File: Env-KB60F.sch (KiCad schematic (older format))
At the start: 125 parts, among them U1 Pico

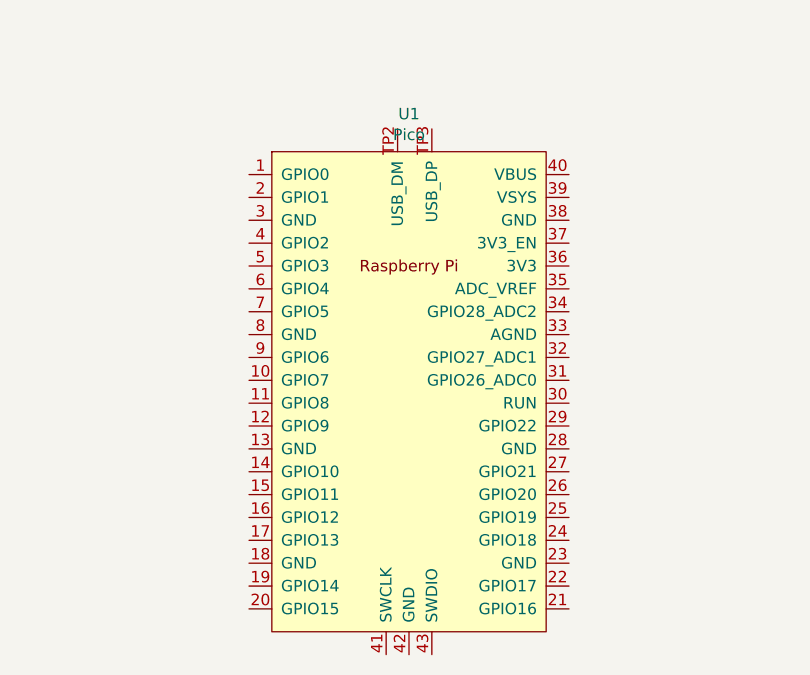
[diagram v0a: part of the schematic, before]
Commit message: Diodes were wrong direction
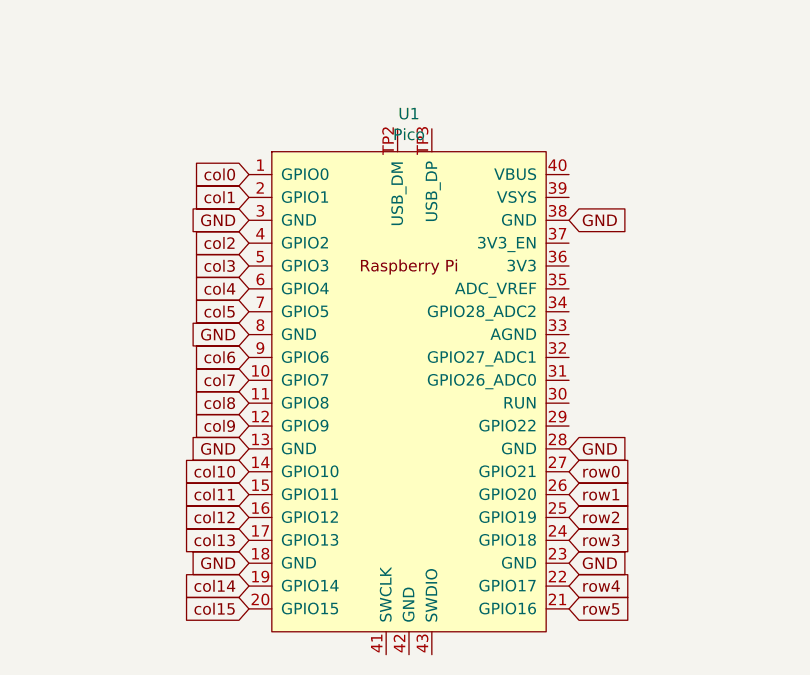
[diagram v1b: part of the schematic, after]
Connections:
- net col0: now also U1.1 (GPIO0)
- net col1: now also U1.2 (GPIO1)
- net col10: now also U1.14 (GPIO10)
- net col11: now also U1.15 (GPIO11)
- net col12: now also U1.16 (GPIO12)
- net col13: now also U1.17 (GPIO13)
- net col14: now also U1.19 (GPIO14)
- net col2: now also U1.4 (GPIO2)
- net col3: now also U1.5 (GPIO3)
- net col4: now also U1.6 (GPIO4)
- net col5: now also U1.7 (GPIO5)
- net col6: now also U1.9 (GPIO6)
- net col7: now also U1.10 (GPIO7)
- net col8: now also U1.11 (GPIO8)
- net col9: now also U1.12 (GPIO9)
- net row0: now also U1.27 (GPIO21)
- net row1: now also U1.26 (GPIO20)
- net row2: now also U1.25 (GPIO19)
- net row3: now also U1.24 (GPIO18)
- net row4: now also U1.22 (GPIO17)
- net GND: now reaches U1.13 (GND)
- net GND: now also U1.18 (GND), U1.23 (GND), U1.28 (GND), U1.3 (GND), U1.38 (GND), U1.8 (GND)
- net col15: now reaches U1.20 (GPIO15)
- net row5: now reaches U1.21 (GPIO16)
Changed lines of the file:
@@
 	1    0    0    -1
 $EndComp
+Text GLabel 3100 6950 0    50   Input ~ 0
+GND
+Text GLabel 3100 7450 0    50   Input ~ 0
+GND
+Text GLabel 3100 7950 0    50   Input ~ 0
+GND
+Text GLabel 3100 6450 0    50   Input ~ 0
+GND
+Text GLabel 4500 6450 2    50   Input ~ 0
+GND
+Text GLabel 4500 7450 2    50   Input ~ 0
+GND
+Text GLabel 4500 7950 2    50   Input ~ 0
+GND
+Text GLabel 4500 7550 2    50   Input ~ 0
+row0
+Text GLabel 4500 7650 2    50   Input ~ 0
+row1
+Text GLabel 4500 7750 2    50   Input ~ 0
+row2
+Text GLabel 4500 7850 2    50   Input ~ 0
+row3
+Text GLabel 4500 8050 2    50   Input ~ 0
+row4
+Text GLabel 4500 8150 2    50   Input ~ 0
+row5
+Text GLabel 3100 6250 0    50   Input ~ 0
+col0
+Text GLabel 3100 6350 0    50   Input ~ 0
+col1
+Text GLabel 3100 6550 0    50   Input ~ 0
+col2
+Text GLabel 3100 6650 0    50   Input ~ 0
+col3
+Text GLabel 3100 6750 0    50   Input ~ 0
+col4
+Text GLabel 3100 6850 0    50   Input ~ 0
+col5
+Text GLabel 3100 7050 0    50   Input ~ 0
+col6
+Text GLabel 3100 7150 0    50   Input ~ 0
+col7
+Text GLabel 3100 7250 0    50   Input ~ 0
+col8
+Text GLabel 3100 7350 0    50   Input ~ 0
+col9
+Text GLabel 3100 7550 0    50   Input ~ 0
+col10
+Text GLabel 3100 7650 0    50   Input ~ 0
+col11
+Text GLabel 3100 7750 0    50   Input ~ 0
+col12
+Text GLabel 3100 7850 0    50   Input ~ 0
+col13
+Text GLabel 3100 8050 0    50   Input ~ 0
+col14
+Text GLabel 3100 8150 0    50   Input ~ 0
+col15
 $EndSCHEMATC

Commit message: General Re-doing of stuff
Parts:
- added H? (x6): MountingHole, symbol Mechanical:MountingHole
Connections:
- net col15 is gone; now on net row4: U1.20 (GPIO15)
- net row5 is gone; now on net col6: U1.21 (GPIO16)
- net col0: now also U1.14 (GPIO10); no longer U1.1 (GPIO0)
- net col1: now also U1.12 (GPIO9); no longer U1.2 (GPIO1)
- net col10: now also U1.26 (GPIO20); no longer U1.14 (GPIO10)
- net col11: now also U1.27 (GPIO21); no longer U1.15 (GPIO11)
- net col12: now also U1.29 (GPIO22); no longer U1.16 (GPIO12)
- net col13: now also U1.31 (GPIO26_ADC0); no longer U1.17 (GPIO13)
- net col14: now also U1.32 (GPIO27_ADC1); no longer U1.19 (GPIO14)
- net col2: now also U1.11 (GPIO8); no longer U1.4 (GPIO2)
- net col3: now also U1.10 (GPIO7); no longer U1.5 (GPIO3)
- net col4: now also U1.9 (GPIO6); no longer U1.6 (GPIO4)
- net col6: no longer U1.9 (GPIO6)
- net col7: now also U1.22 (GPIO17); no longer U1.10 (GPIO7)
- net col8: now also U1.24 (GPIO18); no longer U1.11 (GPIO8)
- net col9: now also U1.25 (GPIO19); no longer U1.12 (GPIO9)
- net row0: now also U1.15 (GPIO11); no longer U1.27 (GPIO21)
- net row1: now also U1.16 (GPIO12); no longer U1.26 (GPIO20)
- net row2: now also U1.17 (GPIO13); no longer U1.25 (GPIO19)
- net row3: now also U1.19 (GPIO14); no longer U1.24 (GPIO18)
- net row4: no longer U1.22 (GPIO17)
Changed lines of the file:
@@
 Text GLabel 4500 7950 2    50   Input ~ 0
 GND
-Text GLabel 4500 7550 2    50   Input ~ 0
+Text GLabel 3100 7650 0    50   Input ~ 0
 row0
-Text GLabel 4500 7650 2    50   Input ~ 0
+Text GLabel 3100 7750 0    50   Input ~ 0
 row1
-Text GLabel 4500 7750 2    50   Input ~ 0
+Text GLabel 3100 7850 0    50   Input ~ 0
 row2
-Text GLabel 4500 7850 2    50   Input ~ 0
+Text GLabel 3100 8050 0    50   Input ~ 0
 row3
-Text GLabel 4500 8050 2    50   Input ~ 0
+Text GLabel 3100 8150 0    50   Input ~ 0
 row4
-Text GLabel 4500 8150 2    50   Input ~ 0
-row5
-Text GLabel 3100 6250 0    50   Input ~ 0
+Text GLabel 3100 7550 0    50   Input ~ 0
 col0
-Text GLabel 3100 6350 0    50   Input ~ 0
+Text GLabel 3100 7350 0    50   Input ~ 0
 col1
-Text GLabel 3100 6550 0    50   Input ~ 0
+Text GLabel 3100 7250 0    50   Input ~ 0
 col2
-Text GLabel 3100 6650 0    50   Input ~ 0
+Text GLabel 3100 7150 0    50   Input ~ 0
 col3
-Text GLabel 3100 6750 0    50   Input ~ 0
+Text GLabel 3100 7050 0    50   Input ~ 0
 col4
 Text GLabel 3100 6850 0    50   Input ~ 0
 col5
-Text GLabel 3100 7050 0    50   Input ~ 0
+Text GLabel 4500 8150 2    50   Input ~ 0
 col6
-Text GLabel 3100 7150 0    50   Input ~ 0
+Text GLabel 4500 8050 2    50   Input ~ 0
 col7
-Text GLabel 3100 7250 0    50   Input ~ 0
+Text GLabel 4500 7850 2    50   Input ~ 0
 col8
-Text GLabel 3100 7350 0    50   Input ~ 0
+Text GLabel 4500 7750 2    50   Input ~ 0
 col9
-Text GLabel 3100 7550 0    50   Input ~ 0
+Text GLabel 4500 7650 2    50   Input ~ 0
 col10
-Text GLabel 3100 7650 0    50   Input ~ 0
+Text GLabel 4500 7550 2    50   Input ~ 0
 col11
-Text GLabel 3100 7750 0    50   Input ~ 0
+Text GLabel 4500 7350 2    50   Input ~ 0
 col12
-Text GLabel 3100 7850 0    50   Input ~ 0
+Text GLabel 4500 7150 2    50   Input ~ 0
 col13
-Text GLabel 3100 8050 0    50   Input ~ 0
+Text GLabel 4500 7050 2    50   Input ~ 0
 col14
-Text GLabel 3100 8150 0    50   Input ~ 0
-col15
+$Comp
+L Mechanical:MountingHole H?
+U 1 1 60A3D400
+P 5600 6350
+F 0 "H?" H 5700 6396 50  0000 L CNN
+F 1 "MountingHole" H 5700 6305 50  0000 L CNN
+F 2 "" H 5600 6350 50  0001 C CNN
+F 3 "~" H 5600 6350 50  0001 C CNN
+	1    5600 6350
+	1    0    0    -1
+$EndComp
+$Comp
+L Mechanical:MountingHole H?
+U 1 1 60A3E33F
+P 5600 6550
+F 0 "H?" H 5700 6596 50  0000 L CNN
+F 1 "MountingHole" H 5700 6505 50  0000 L CNN
+F 2 "" H 5600 6550 50  0001 C CNN
+F 3 "~" H 5600 6550 50  0001 C CNN
+	1    5600 6550
+	1    0    0    -1
+$EndComp
+$Comp
+L Mechanical:MountingHole H?
+U 1 1 60A4E76C
+P 5600 6750
+F 0 "H?" H 5700 6796 50  0000 L CNN
+F 1 "MountingHole" H 5700 6705 50  0000 L CNN
+F 2 "" H 5600 6750 50  0001 C CNN
+F 3 "~" H 5600 6750 50  0001 C CNN
+	1    5600 6750
+	1    0    0    -1
+$EndComp
+$Comp
+L Mechanical:MountingHole H?
+U 1 1 60A5EC63
+P 5600 6950
+F 0 "H?" H 5700 6996 50  0000 L CNN
+F 1 "MountingHole" H 5700 6905 50  0000 L CNN
+F 2 "" H 5600 6950 50  0001 C CNN
+F 3 "~" H 5600 6950 50  0001 C CNN
+	1    5600 6950
+	1    0    0    -1
+$EndComp
+$Comp
+L Mechanical:MountingHole H?
+U 1 1 60A6F0BC
+P 5600 7150
+F 0 "H?" H 5700 7196 50  0000 L CNN
+F 1 "MountingHole" H 5700 7105 50  0000 L CNN
+F 2 "" H 5600 7150 50  0001 C CNN
+F 3 "~" H 5600 7150 50  0001 C CNN
+	1    5600 7150
+	1    0    0    -1
+$EndComp
+$Comp
+L Mechanical:MountingHole H?
+U 1 1 60A7F4B8
+P 5600 7350
+F 0 "H?" H 5700 7396 50  0000 L CNN
+F 1 "MountingHole" H 5700 7305 50  0000 L CNN
+F 2 "" H 5600 7350 50  0001 C CNN
+F 3 "~" H 5600 7350 50  0001 C CNN
+	1    5600 7350
+	1    0    0    -1
+$EndComp
 $EndSCHEMATC

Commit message: Added some mount holes n stuff
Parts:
- removed H? (x6): MountingHole, symbol Mechanical:MountingHole
- added H1, H2, H3, H4, H5, H6, H7: MountingHole, MountingHole:MountingHole_2.2mm_M2, symbol Mechanical:MountingHole
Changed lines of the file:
@@
 col14
 $Comp
-L Mechanical:MountingHole H?
-U 1 1 60A3D400
+L logo:LOGO #G1
+U 1 1 60871C59
+P 5350 8550
+F 0 "#G1" H 5350 8215 60  0001 C CNN
+F 1 "LOGO" H 5350 8885 60  0001 C CNN
+F 2 "AKLogo:logo" H 5345 8881 50  0000 C CNN
+F 3 "" H 5350 8550 50  0001 C CNN
+	1    5350 8550
+	1    0    0    -1
+$EndComp
+$Comp
+L Mechanical:MountingHole H1
+U 1 1 608AB119
 P 5600 6350
-F 0 "H?" H 5700 6396 50  0000 L CNN
+F 0 "H1" H 5700 6396 50  0000 L CNN
 F 1 "MountingHole" H 5700 6305 50  0000 L CNN
-F 2 "" H 5600 6350 50  0001 C CNN
+F 2 "MountingHole:MountingHole_2.2mm_M2" H 5600 6350 50  0001 C CNN
 F 3 "~" H 5600 6350 50  0001 C CNN
 	1    5600 6350
@@
 $EndComp
 $Comp
-L Mechanical:MountingHole H?
-U 1 1 60A3E33F
+L Mechanical:MountingHole H2
+U 1 1 608ACB73
 P 5600 6550
-F 0 "H?" H 5700 6596 50  0000 L CNN
+F 0 "H2" H 5700 6596 50  0000 L CNN
 F 1 "MountingHole" H 5700 6505 50  0000 L CNN
-F 2 "" H 5600 6550 50  0001 C CNN
+F 2 "MountingHole:MountingHole_2.2mm_M2" H 5600 6550 50  0001 C CNN
 F 3 "~" H 5600 6550 50  0001 C CNN
 	1    5600 6550
@@
 $EndComp
 $Comp
-L Mechanical:MountingHole H?
-U 1 1 60A4E76C
+L Mechanical:MountingHole H3
+U 1 1 608BCF9C
 P 5600 6750
-F 0 "H?" H 5700 6796 50  0000 L CNN
+F 0 "H3" H 5700 6796 50  0000 L CNN
 F 1 "MountingHole" H 5700 6705 50  0000 L CNN
-F 2 "" H 5600 6750 50  0001 C CNN
+F 2 "MountingHole:MountingHole_2.2mm_M2" H 5600 6750 50  0001 C CNN
 F 3 "~" H 5600 6750 50  0001 C CNN
 	1    5600 6750
@@
 $EndComp
 $Comp
-L Mechanical:MountingHole H?
-U 1 1 60A5EC63
+L Mechanical:MountingHole H4
+U 1 1 608CD285
 P 5600 6950
-F 0 "H?" H 5700 6996 50  0000 L CNN
+F 0 "H4" H 5700 6996 50  0000 L CNN
 F 1 "MountingHole" H 5700 6905 50  0000 L CNN
-F 2 "" H 5600 6950 50  0001 C CNN
+F 2 "MountingHole:MountingHole_2.2mm_M2" H 5600 6950 50  0001 C CNN
 F 3 "~" H 5600 6950 50  0001 C CNN
 	1    5600 6950
@@
 $EndComp
 $Comp
-L Mechanical:MountingHole H?
-U 1 1 60A6F0BC
+L Mechanical:MountingHole H5
+U 1 1 608DD691
 P 5600 7150
-F 0 "H?" H 5700 7196 50  0000 L CNN
+F 0 "H5" H 5700 7196 50  0000 L CNN
 F 1 "MountingHole" H 5700 7105 50  0000 L CNN
-F 2 "" H 5600 7150 50  0001 C CNN
+F 2 "MountingHole:MountingHole_2.2mm_M2" H 5600 7150 50  0001 C CNN
 F 3 "~" H 5600 7150 50  0001 C CNN
 	1    5600 7150
@@
 $EndComp
 $Comp
-L Mechanical:MountingHole H?
-U 1 1 60A7F4B8
+L Mechanical:MountingHole H6
+U 1 1 608EDB63
 P 5600 7350
-F 0 "H?" H 5700 7396 50  0000 L CNN
+F 0 "H6" H 5700 7396 50  0000 L CNN
 F 1 "MountingHole" H 5700 7305 50  0000 L CNN
-F 2 "" H 5600 7350 50  0001 C CNN
+F 2 "MountingHole:MountingHole_2.2mm_M2" H 5600 7350 50  0001 C CNN
 F 3 "~" H 5600 7350 50  0001 C CNN
 	1    5600 7350
 	1    0    0    -1
 $EndComp
+$Comp
+L Mechanical:MountingHole H7
+U 1 1 609431FD
+P 5600 7550
+F 0 "H7" H 5700 7596 50  0000 L CNN
+F 1 "MountingHole" H 5700 7505 50  0000 L CNN
+F 2 "MountingHole:MountingHole_2.2mm_M2" H 5600 7550 50  0001 C CNN
+F 3 "~" H 5600 7550 50  0001 C CNN
+	1    5600 7550
+	1    0    0    -1
+$EndComp

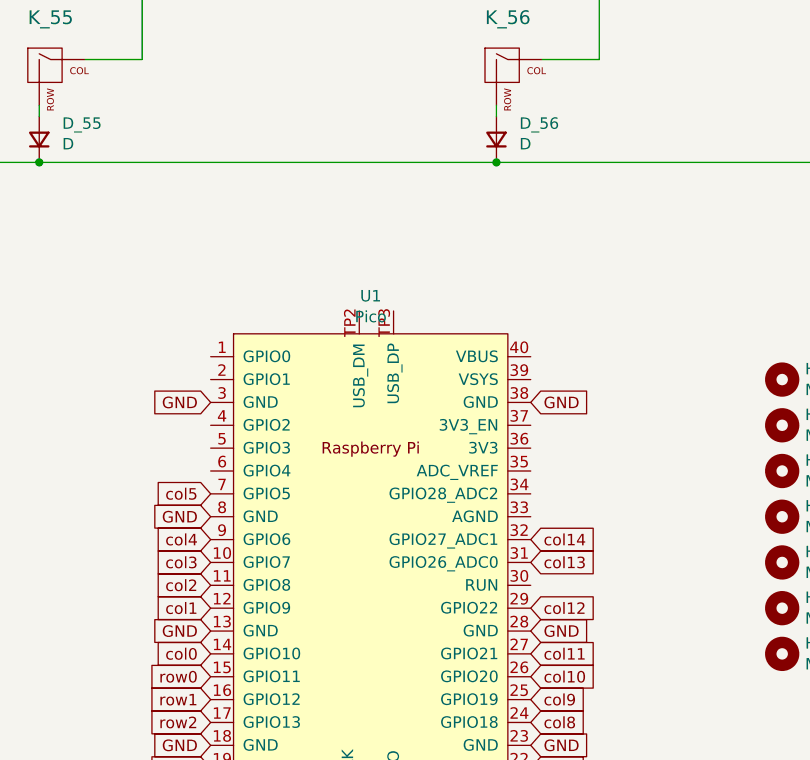
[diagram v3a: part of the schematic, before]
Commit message: Added some stuff
Added a Button for reset and also a bunch of silkscreen instructions for building the keyboard aswell as a QR Code URL that brings you to this Repository.
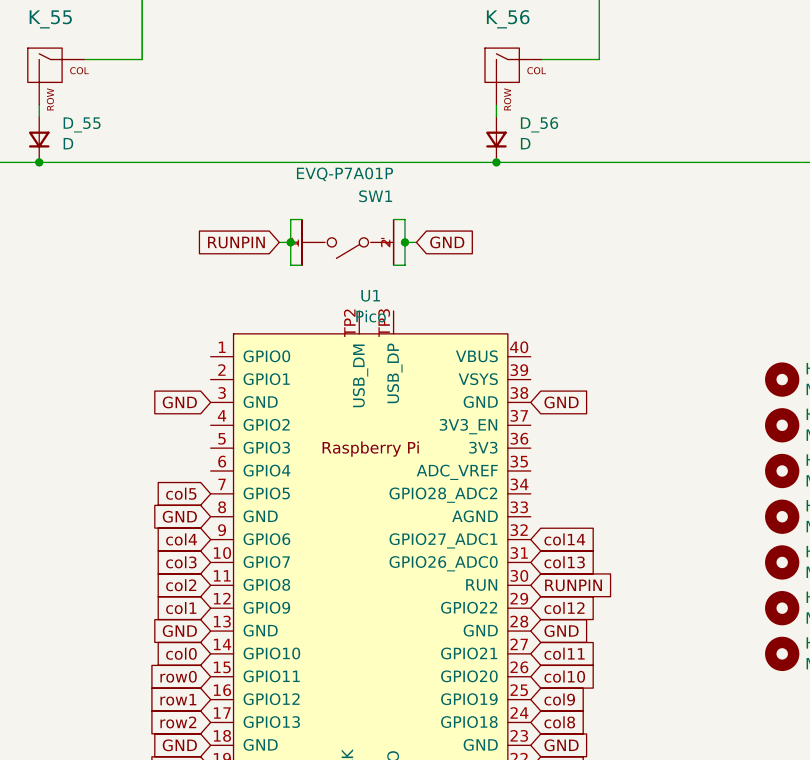
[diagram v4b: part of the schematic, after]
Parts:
- added SW1: EVQ-P7A01P, PanasonicEVQ-P7A01P:Panasonic-EVQ-P7A01P-0-0-MFG, symbol PanasonicEVQ-P7A01P:EVQ-P7A01P
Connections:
- net GND: now also SW1.2, SW1.2'
- net RUNPIN: now reaches U1.30 (RUN)
- net RUNPIN: now also SW1.1, SW1.1'
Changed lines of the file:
@@
 	1    0    0    -1
 $EndComp
+Text GLabel 4500 7250 2    50   Input ~ 0
+RUNPIN
+Text GLabel 3400 5750 0    50   Input ~ 0
+RUNPIN
+Text GLabel 4000 5750 2    50   Input ~ 0
+GND
+$Comp
+L PanasonicEVQ-P7A01P:EVQ-P7A01P SW1
+U 1 1 6096F576
+P 3900 5950
+F 0 "SW1" H 3900 5550 50  0000 L CNN
+F 1 "EVQ-P7A01P" H 3900 5450 50  0000 L CNN
+F 2 "PanasonicEVQ-P7A01P:Panasonic-EVQ-P7A01P-0-0-MFG" H 3900 6150 50  0001 L CNN
+F 3 "https://industrial.panasonic.com/cdbs/www-data/pdf/ATK0000/ATK0000C378.pdf" H 3900 6250 50  0001 L CNN
+F 4 "No" H 3900 6350 50  0001 L CNN "automotive"
+F 5 "Switch" H 3900 6450 50  0001 L CNN "category"
+F 6 "50mA" H 3900 6550 50  0001 L CNN "contact current rating"
+F 7 "500mΩ" H 3900 6650 50  0001 L CNN "contact resistance"
+F 8 "Electromechanical" H 3900 6750 50  0001 L CNN "device class L1"
+F 9 "Switches" H 3900 6850 50  0001 L CNN "device class L2"
+F 10 "Tactile Switches" H 3900 6950 50  0001 L CNN "device class L3"
+F 11 "SWITCH TACTILE SPST-NO 0.05A 12V" H 3900 7050 50  0001 L CNN "digikey description"
+F 12 "P16763CT-ND" H 3900 7150 50  0001 L CNN "digikey part number"
+F 13 "100000Cycles" H 3900 7250 50  0001 L CNN "electromechanical life"
+F 14 "1.55mm" H 3900 7350 50  0001 L CNN "height"
+F 15 "Yes" H 3900 7450 50  0001 L CNN "lead free"
+F 16 "2f293019bba4f771" H 3900 7550 50  0001 L CNN "library id"
+F 17 "Panasonic" H 3900 7650 50  0001 L CNN "manufacturer"
+F 18 "Surface Mount" H 3900 7750 50  0001 L CNN "mount"
+F 19 "SWITCH TACTILE SPST-NO 0.05A 12V" H 3900 7850 50  0001 L CNN "mouser description"
+F 20 "667-EVQP7A01P" H 3900 7950 50  0001 L CNN "mouser part number"
+F 21 "2.2N" H 3900 8050 50  0001 L CNN "operating force"
+F 22 "SMT_SW_3MM5_2MM9" H 3900 8150 50  0001 L CNN "package"
+F 23 "Yes" H 3900 8250 50  0001 L CNN "rohs"
+F 24 "+70°C" H 3900 8350 50  0001 L CNN "temperature range high"
+F 25 "-20°C" H 3900 8450 50  0001 L CNN "temperature range low"
+F 26 "SPST-NO" H 3900 8550 50  0001 L CNN "throw configuration"
+F 27 "12V" H 3900 8650 50  0001 L CNN "voltage rating DC"
+	1    3900 5950
+	-1   0    0    1
+$EndComp
+Wire Wire Line
+	3400 5750 3450 5750
+Wire Wire Line
+	3450 5750 3450 5650
+Wire Wire Line
+	3450 5650 3500 5650
+Wire Wire Line
+	3450 5750 3450 5850
+Wire Wire Line
+	3450 5850 3500 5850
+Connection ~ 3450 5750
+Wire Wire Line
+	3900 5850 3950 5850
+Wire Wire Line
+	3900 5650 3950 5650
+Wire Wire Line
+	3950 5650 3950 5750
+Wire Wire Line
+	4000 5750 3950 5750
+Connection ~ 3950 5750
+Wire Wire Line
+	3950 5750 3950 5850
 $EndSCHEMATC

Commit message: Mount hole adjustments
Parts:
- added H10, H8, H9: MountingHole, MountingHole:MountingHole_2.2mm_M2, symbol Mechanical:MountingHole
- added H11: MountingHole, MountingHole:MountingHole_2.1mm, symbol Mechanical:MountingHole
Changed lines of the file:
@@
 Wire Wire Line
 	3950 5750 3950 5850
+$Comp
+L Mechanical:MountingHole H8
+U 1 1 609389EF
+P 6400 6350
+F 0 "H8" H 6500 6396 50  0000 L CNN
+F 1 "MountingHole" H 6500 6305 50  0000 L CNN
+F 2 "MountingHole:MountingHole_2.2mm_M2" H 6400 6350 50  0001 C CNN
+F 3 "~" H 6400 6350 50  0001 C CNN
+	1    6400 6350
+	1    0    0    -1
+$EndComp
+$Comp
+L Mechanical:MountingHole H9
+U 1 1 609389F5
+P 6400 6550
+F 0 "H9" H 6500 6596 50  0000 L CNN
+F 1 "MountingHole" H 6500 6505 50  0000 L CNN
+F 2 "MountingHole:MountingHole_2.2mm_M2" H 6400 6550 50  0001 C CNN
+F 3 "~" H 6400 6550 50  0001 C CNN
+	1    6400 6550
+	1    0    0    -1
+$EndComp
+$Comp
+L Mechanical:MountingHole H10
+U 1 1 609389FB
+P 6400 6750
+F 0 "H10" H 6500 6796 50  0000 L CNN
+F 1 "MountingHole" H 6500 6705 50  0000 L CNN
+F 2 "MountingHole:MountingHole_2.2mm_M2" H 6400 6750 50  0001 C CNN
+F 3 "~" H 6400 6750 50  0001 C CNN
+	1    6400 6750
+	1    0    0    -1
+$EndComp
+$Comp
+L Mechanical:MountingHole H11
+U 1 1 60938A01
+P 6400 6950
+F 0 "H11" H 6500 6996 50  0000 L CNN
+F 1 "MountingHole" H 6500 6905 50  0000 L CNN
+F 2 "MountingHole:MountingHole_2.1mm" H 6400 6950 50  0001 C CNN
+F 3 "~" H 6400 6950 50  0001 C CNN
+	1    6400 6950
+	1    0    0    -1
+$EndComp
 $EndSCHEMATC

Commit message: Added ANSI Left Shift, Enter and Backslash
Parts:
- removed D_0: D, Diode_THT:D_DO-35_SOD27_P7.62mm_Horizontal, symbol Device:D_Small
- added D_1, D_28: D, Diode_THT:D_DO-35_SOD27_P7.62mm_Horizontal, symbol Device:D_Small
- added K_28: KEYSW, MX_Only:MXOnly-1.5U-NoLED, symbol MX_Alps_Hybrid:MX-NoLED
- added K_29, K_44: KEYSW, MX_Only:MXOnly-2.25U-NoLED, symbol MX_Alps_Hybrid:MX-NoLED
- renumbered D_9 to D_10, D_10 to D_11, D_11 to D_12, D_12 to D_13, D_13 to D_14, D_14 to D_15, D_15 to D_16, D_16 to D_17, D_17 to D_18, D_18 to D_19, D_1 to D_2, D_19 to D_20, D_20 to D_21, D_21 to D_22, D_22 to D_23, D_23 to D_24, D_24 to D_25, D_25 to D_26, D_26 to D_27, D_27 to D_29, D_2 to D_3, D_28 to D_30, D_29 to D_31, D_30 to D_32, D_31 to D_33, D_32 to D_34, D_33 to D_35, D_34 to D_36, D_35 to D_37, D_36 to D_38, D_37 to D_39, D_3 to D_4, D_38 to D_40, D_39 to D_41, D_40 to D_42, D_41 to D_43, D_42 to D_44, D_43 to D_45, D_44 to D_46, D_45 to D_47, D_46 to D_48, D_47 to D_49, D_4 to D_5, D_48 to D_50, D_49 to D_51, D_50 to D_52, D_51 to D_53, D_52 to D_54, D_53 to D_55, D_54 to D_56, D_55 to D_57, D_56 to D_58, D_57 to D_59, D_5 to D_6, D_58 to D_60, D_59 to D_61, D_60 to D_62, D_61 to D_63, D_6 to D_7, D_7 to D_8, D_8 to D_9, H6 to H10, H7 to H11, H8 to H2, H2 to H3, H9 to H4, H3 to H5, H10 to H6, H4 to H7, H11 to H8, H5 to H9, K_0 to K_1, K_9 to K_10, K_10 to K_11, K_11 to K_12, K_12 to K_13, K_13 to K_14, K_14 to K_15, K_15 to K_16, K_16 to K_17, K_17 to K_18, K_18 to K_19, K_1 to K_2, K_19 to K_20, K_20 to K_21, K_21 to K_22, K_22 to K_23, K_23 to K_24, K_24 to K_25, K_25 to K_26, K_26 to K_27, K_2 to K_3, K_27 to K_30, K_28 to K_31, K_29 to K_32, K_30 to K_33, K_31 to K_34, K_32 to K_35, K_33 to K_36, K_34 to K_37, K_35 to K_38, K_36 to K_39, K_3 to K_4, K_37 to K_40, K_38 to K_41, K_39 to K_42, K_40 to K_43, K_41 to K_45, K_42 to K_46, K_43 to K_47, K_44 to K_48, K_45 to K_49, K_4 to K_5, K_46 to K_50, K_47 to K_51, K_48 to K_52, K_49 to K_53, K_50 to K_54, K_51 to K_55, K_52 to K_56, K_53 to K_57, K_54 to K_58, K_55 to K_59, K_5 to K_6, K_56 to K_60, K_57 to K_61, K_58 to K_62, K_59 to K_63, K_60 to K_64, K_61 to K_65, K_6 to K_7, K_7 to K_8, K_8 to K_9
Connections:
- net col0: now also K_44.1 (COL)
- net col14: now also K_28.1 (COL), K_29.1 (COL)
- net row0: now also D_1.1 (K)
- net row1: now also D_28.1 (K)
- net at K_1.2 (ROW): now also D_1.2 (A)
- net at D_42.2 (A), K_43.2 (ROW): now also K_29.2 (ROW)
- net at D_43.2 (A), K_45.2 (ROW): now also K_44.2 (ROW)
- new net: D_28.2 (A), K_28.2 (ROW)
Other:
- note added: "ANSI Enter"
- note added: "ANSI Left Shift"
- note added: "ANSI backslash"
